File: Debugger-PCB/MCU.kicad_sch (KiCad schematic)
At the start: 12 parts, among them U5 STM32F103RCTx, Y1 12M

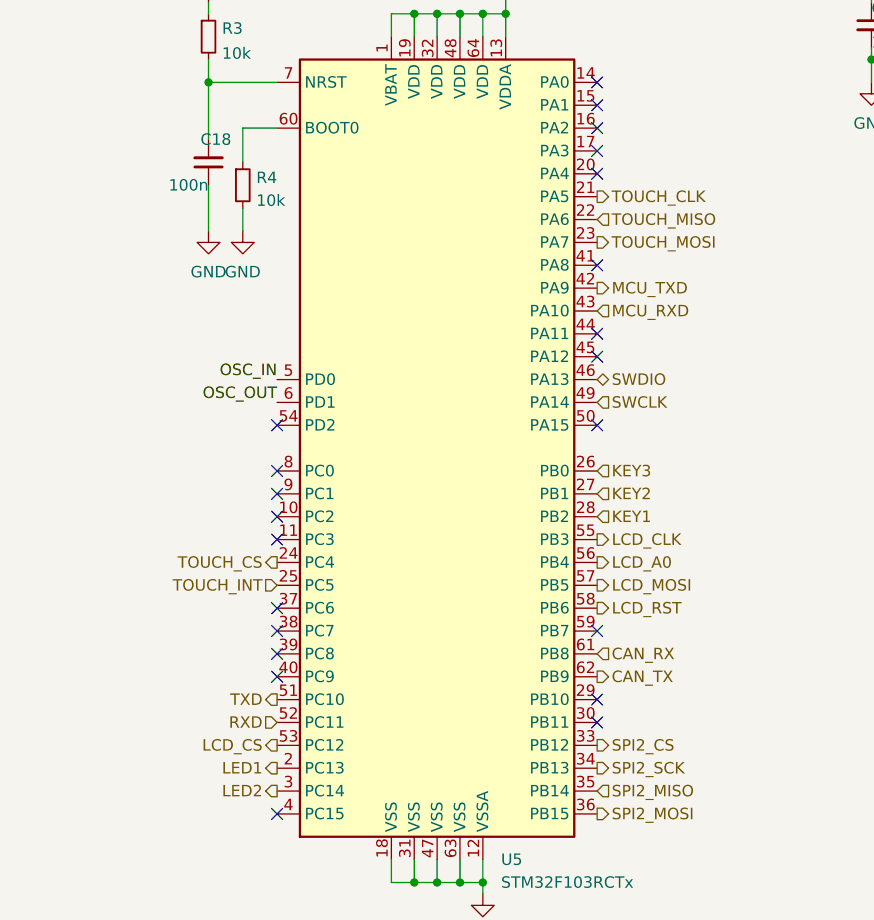
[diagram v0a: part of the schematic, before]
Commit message: fix some details of PCB
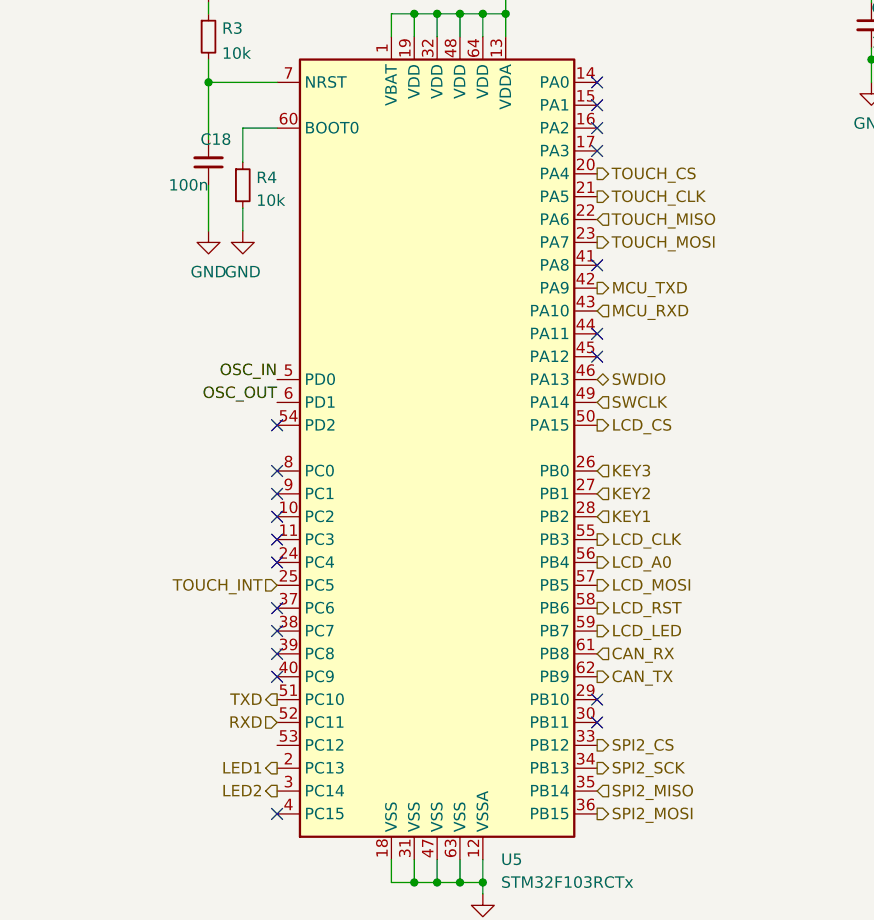
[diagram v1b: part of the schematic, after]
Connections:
- net LCD_CS: now also U5.50 (PA15); no longer U5.53 (PC12)
- net TOUCH_CS: now also U5.20 (PA4); no longer U5.24 (PC4)
- net LCD_LED: now reaches U5.59 (PB7)
- no-connect marks 22 -> 20
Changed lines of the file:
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@@
   (junction (at 134.62 43.18) (diameter 0) (color 0 0 0 0)
   )
-  (no_connect (at 152.4 111.76))
   (no_connect (at 116.84 96.52))
-  (no_connect (at 152.4 88.9))
   (no_connect (at 152.4 55.88))
   (no_connect (at 116.84 109.22))
   (no_connect (at 116.84 111.76))
+  (no_connect (at 116.84 104.14))
   (no_connect (at 116.84 101.6))
   (no_connect (at 152.4 81.28))
@@
   (no_connect (at 116.84 114.3))
   (no_connect (at 152.4 58.42))
-  (no_connect (at 152.4 60.96))
   (no_connect (at 152.4 119.38))
   (no_connect (at 116.84 93.98))
@@
     (effects (font (size 1.27 1.27)) (justify left))
   )
+  (hierarchical_label "LCD_LED" (shape output) (at 152.4 111.76 0)
+    (effects (font (size 1.27 1.27)) (justify left))
+  )
   (hierarchical_label "TXD" (shape output) (at 116.84 119.38 180)
     (effects (font (size 1.27 1.27)) (justify right))
@@
     (effects (font (size 1.27 1.27)) (justify left))
   )
+  (hierarchical_label "LCD_CS" (shape output) (at 152.4 88.9 0)
+    (effects (font (size 1.27 1.27)) (justify left))
+  )
   (hierarchical_label "SWDIO" (shape bidirectional) (at 152.4 83.82 0)
     (effects (font (size 1.27 1.27)) (justify left))
@@
     (effects (font (size 1.27 1.27)) (justify left))
   )
-  (hierarchical_label "TOUCH_CS" (shape output) (at 116.84 104.14 180)
-    (effects (font (size 1.27 1.27)) (justify right))
-  )
   (hierarchical_label "CAN_RX" (shape input) (at 152.4 114.3 0)
     (effects (font (size 1.27 1.27)) (justify left))
@@
   )
   (hierarchical_label "TOUCH_MISO" (shape input) (at 152.4 66.04 0)
+    (effects (font (size 1.27 1.27)) (justify left))
+  )
+  (hierarchical_label "TOUCH_CS" (shape output) (at 152.4 60.96 0)
     (effects (font (size 1.27 1.27)) (justify left))
   )
@@
     (effects (font (size 1.27 1.27)) (justify left))
   )
-  (hierarchical_label "LCD_CS" (shape output) (at 116.84 124.46 180)
-    (effects (font (size 1.27 1.27)) (justify right))
-  )
   (hierarchical_label "KEY1" (shape input) (at 152.4 99.06 0)

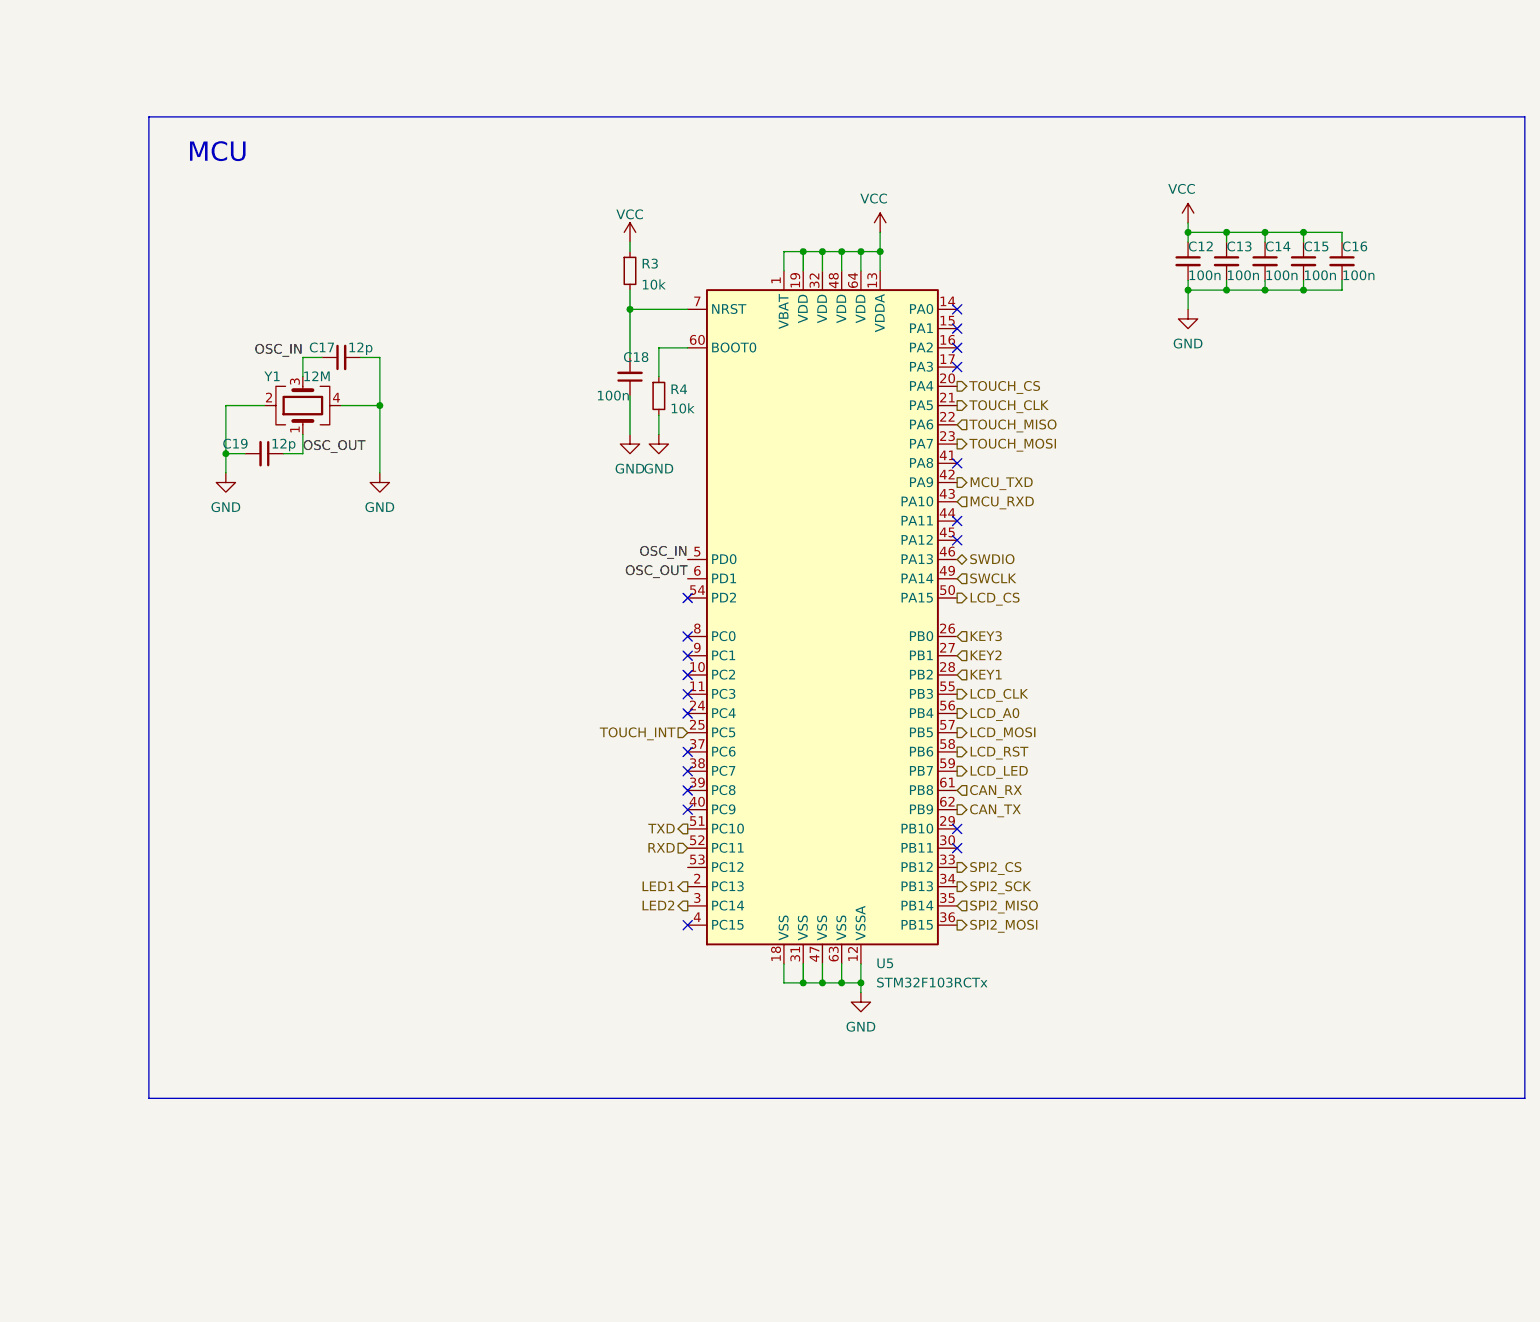
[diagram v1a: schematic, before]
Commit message: change the file name debugger-code into debugger_code_f103. Change the stm32f103rct6 into stm32f407vet6. Add file debugger_code_f407
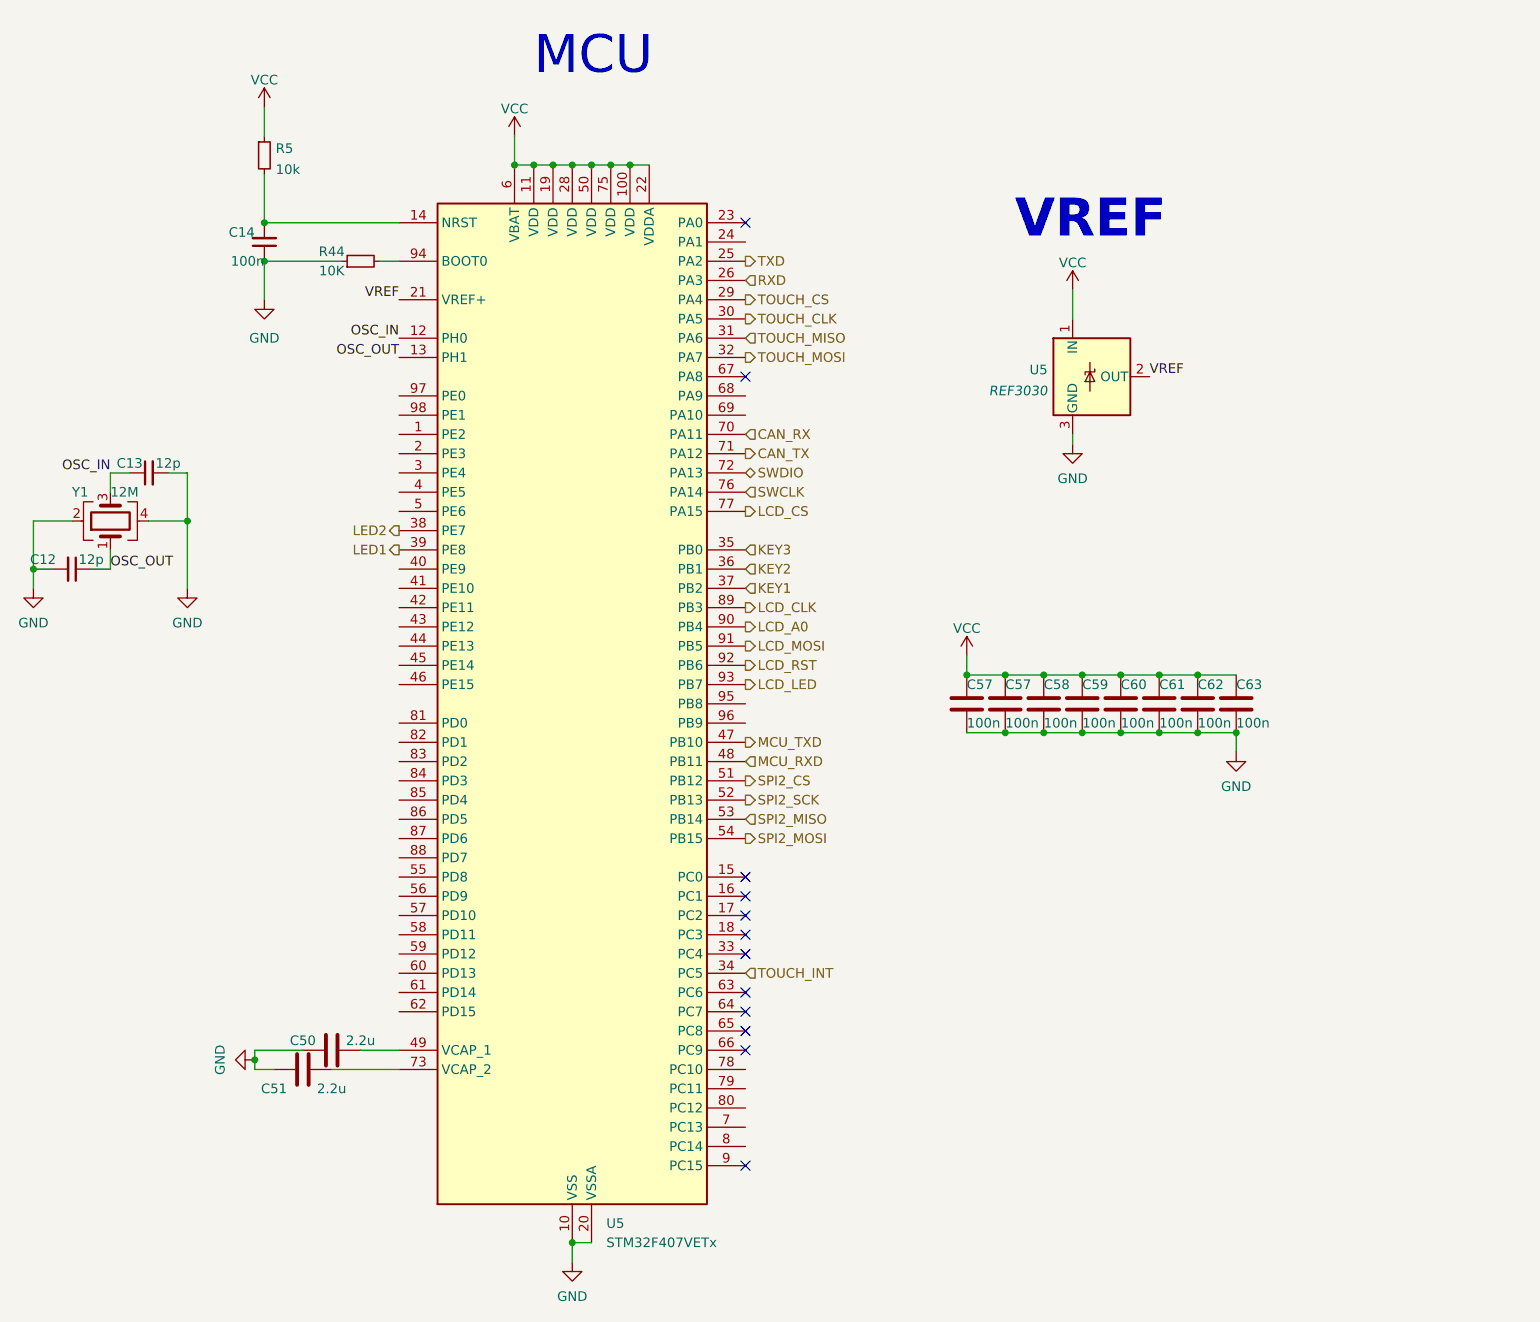
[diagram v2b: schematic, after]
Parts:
- removed C15, C16, C18: 100n, Capacitor_SMD:C_0603_1608Metric, symbol Device:C_Small
- removed C17, C19: 12p, Capacitor_SMD:C_0603_1608Metric, symbol Device:C_Small
- removed R3, R4: 10k, Resistor_SMD:R_0603_1608Metric, symbol Device:R_Small
- removed U5: STM32F103RCTx, Package_QFP:LQFP-64_10x10mm_P0.5mm, symbol MCU_ST_STM32F1:STM32F103RCTx
- added C50, C51: 2.2u, Capacitor_SMD:C_0603_1608Metric, symbol Device:C
- added C57 (x2), C58, C59, C60, C61, C62, C63: 100n, Capacitor_SMD:C_0603_1608Metric, symbol Device:C
- added R44: 10K, Resistor_SMD:R_0603_1608Metric, symbol Device:R_Small
- added R5: 10k, Resistor_SMD:R_0603_1608Metric, symbol Device:R_Small
- added U5: STM32F407VETx, Package_QFP:LQFP-100_14x14mm_P0.5mm, symbol MCU_ST_STM32F4:STM32F407VETx
- added U5: REF3030, Package_TO_SOT_SMD:SOT-23, symbol Reference_Voltage:REF3030
- C12, C13: value 100n -> 12p
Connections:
- net CAN_RX: now also U5.70 (PA11)
- net CAN_TX: now also U5.71 (PA12)
- net GND: now also C14.1, C50.1, C51.1, C57.2, C57.2, C58.2, C59.2, C60.2, C61.2, C62.2, C63.2, R44.1, U5.10 (VSS), U5.20 (VSSA), U5.27 (VSS), U5.3 (GND), U5.74 (VSS), U5.99 (VSS); no longer C14.2
- net KEY1: now also U5.37 (PB2)
- net KEY2: now also U5.36 (PB1)
- net KEY3: now also U5.35 (PB0)
- net LCD_A0: now also U5.90 (PB4)
- net LCD_CLK: now also U5.89 (PB3)
- net LCD_CS: now also U5.77 (PA15)
- net LCD_LED: now also U5.93 (PB7)
- net LCD_MOSI: now also U5.91 (PB5)
- net LCD_RST: now also U5.92 (PB6)
- net LED1: now also U5.39 (PE8)
- net LED2: now also U5.38 (PE7)
- net MCU_RXD: now also U5.48 (PB11)
- net MCU_TXD: now also U5.47 (PB10)
- net OSC_IN: now also C13.1, U5.12 (PH0)
- net OSC_OUT: now also C12.1, U5.13 (PH1)
- net RXD: now also U5.26 (PA3)
- net SPI2_CS: now also U5.51 (PB12)
- net SPI2_MISO: now also U5.53 (PB14)
- net SPI2_MOSI: now also U5.54 (PB15)
- net SPI2_SCK: now also U5.52 (PB13)
- net SWCLK: now also U5.76 (PA14)
- net SWDIO: now also U5.72 (PA13)
- net TOUCH_CLK: now also U5.30 (PA5)
- net TOUCH_CS: now also U5.29 (PA4)
- net TOUCH_INT: now also U5.34 (PC5)
- net TOUCH_MISO: now also U5.31 (PA6)
- net TOUCH_MOSI: now also U5.32 (PA7)
- net TXD: now also U5.25 (PA2)
- net VCC: now also C57.1, C57.1, C58.1, C59.1, C60.1, C61.1, C62.1, C63.1, R5.1, U5.1 (IN), U5.100 (VDD), U5.11 (VDD), U5.19 (VDD), U5.22 (VDDA), U5.28 (VDD), U5.50 (VDD), U5.6 (VBAT), U5.75 (VDD); no longer C12.1, C13.1, C14.1
- new net: C14.2, R5.2, U5.14 (NRST)
- new net: C50.2, U5.49 (VCAP_1)
- new net: C51.2, U5.73 (VCAP_2)
- new net: R44.2, U5.94 (BOOT0)
- new net VREF: U5.2 (OUT), U5.21 (VREF+)
- no-connect marks 20 -> 12
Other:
- note added: "VREF"

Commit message: temp.change the PCB.And change the code.
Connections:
- net LCD_CS: now also U5.95 (PB8)
- net RESET: now reaches C14.2, R5.2, U5.14 (NRST)
- net LCD_CS0: now reaches U5.15 (PC0)
- net ADC1_IN11: now reaches U5.16 (PC1)
- net ADC1_IN12: now reaches U5.17 (PC2)
- net ADC1_IN13: now reaches U5.18 (PC3)
- net ADC1_IN0: now reaches U5.23 (PA0)
- net ADC1_IN1: now reaches U5.24 (PA1)
- net ADC1_IN14: now reaches U5.33 (PC4)
- net TIM1_CH1: now reaches U5.40 (PE9)
- net TIM1_CH2: now reaches U5.42 (PE11)
- net I2C3_SDA: now reaches U5.56 (PD9)
- net TIM4_CH2: now reaches U5.59 (PD12)
- net TIM4_CH1: now reaches U5.60 (PD13)
- net TIM3_CH1: now reaches U5.63 (PC6)
- net TIM3_CH2: now reaches U5.64 (PC7)
- net I2C3_SCL: now reaches U5.67 (PA8)
- net KEY5: now reaches U5.68 (PA9)
- net KEY4: now reaches U5.69 (PA10)
- net LCD_DC: now reaches U5.96 (PB9)
- no-connect marks 12 -> 3
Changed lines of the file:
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@@
   (junction (at 173.99 99.06) (diameter 0) (color 0 0 0 0)
   )
-  (no_connect (at 124.46 133.35))
   (no_connect (at 124.46 148.59))
-  (no_connect (at 124.46 39.37))
   (no_connect (at 124.46 146.05))
   (no_connect (at 124.46 163.83))
-  (no_connect (at 124.46 59.69))
-  (no_connect (at 124.46 125.73))
-  (no_connect (at 124.46 140.97))
-  (no_connect (at 124.46 128.27))
-  (no_connect (at 124.46 143.51))
-  (no_connect (at 124.46 135.89))
-  (no_connect (at 124.46 130.81))
   (wire (pts (xy 184.15 106.68) (xy 189.23 106.68))
     (stroke (width 0) (type default))
@@
     (effects (font (size 1.27 1.27)) (justify left))
   )
+  (hierarchical_label "ADC1_IN1" (shape input) (at 124.46 41.91 0) (fields_autoplaced)
+    (effects (font (size 1.27 1.27)) (justify left))
+  )
+  (hierarchical_label "I2C3_SCL" (shape output) (at 124.46 59.69 0) (fields_autoplaced)
+    (effects (font (size 1.27 1.27)) (justify left))
+  )
   (hierarchical_label "SWDIO" (shape bidirectional) (at 124.46 72.39 0) (fields_autoplaced)
     (effects (font (size 1.27 1.27)) (justify left))
@@
     (effects (font (size 1.27 1.27)) (justify left))
   )
+  (hierarchical_label "TIM3_CH1" (shape input) (at 124.46 140.97 0) (fields_autoplaced)
+    (effects (font (size 1.27 1.27)) (justify left))
+  )
+  (hierarchical_label "LCD_DC" (shape output) (at 124.46 105.41 0) (fields_autoplaced)
+    (effects (font (size 1.27 1.27)) (justify left))
+  )
+  (hierarchical_label "KEY5" (shape input) (at 124.46 62.23 0) (fields_autoplaced)
+    (effects (font (size 1.27 1.27)) (justify left))
+  )
+  (hierarchical_label "ADC1_IN14" (shape input) (at 124.46 135.89 0) (fields_autoplaced)
+    (effects (font (size 1.27 1.27)) (justify left))
+  )
+  (hierarchical_label "ADC1_IN13" (shape input) (at 124.46 133.35 0) (fields_autoplaced)
+    (effects (font (size 1.27 1.27)) (justify left))
+  )
   (hierarchical_label "MCU_TXD" (shape output) (at 124.46 107.95 0) (fields_autoplaced)
     (effects (font (size 1.27 1.27)) (justify left))
@@
     (effects (font (size 1.27 1.27)) (justify left))
   )
+  (hierarchical_label "I2C3_SDA" (shape bidirectional) (at 78.74 128.27 180) (fields_autoplaced)
+    (effects (font (size 1.27 1.27)) (justify right))
+  )
+  (hierarchical_label "RESET" (shape input) (at 60.96 39.37 180) (fields_autoplaced)
+    (effects (font (size 1.27 1.27)) (justify right))
+  )
   (hierarchical_label "TOUCH_CS" (shape output) (at 124.46 49.53 0) (fields_autoplaced)
     (effects (font (size 1.27 1.27)) (justify left))
@@
     (effects (font (size 1.27 1.27)) (justify right))
   )
+  (hierarchical_label "ADC1_IN11" (shape input) (at 124.46 128.27 0) (fields_autoplaced)
+    (effects (font (size 1.27 1.27)) (justify left))
+  )
+  (hierarchical_label "ADC1_IN12" (shape input) (at 124.46 130.81 0) (fields_autoplaced)
+    (effects (font (size 1.27 1.27)) (justify left))
+  )
   (hierarchical_label "KEY1" (shape input) (at 124.46 87.63 0) (fields_autoplaced)
     (effects (font (size 1.27 1.27)) (justify left))
   )
+  (hierarchical_label "KEY4" (shape input) (at 124.46 64.77 0) (fields_autoplaced)
+    (effects (font (size 1.27 1.27)) (justify left))
+  )
   (hierarchical_label "CAN_TX" (shape output) (at 124.46 69.85 0) (fields_autoplaced)
     (effects (font (size 1.27 1.27)) (justify left))
@@
     (effects (font (size 1.27 1.27)) (justify left))
   )
+  (hierarchical_label "TIM4_CH1" (shape input) (at 78.74 138.43 180) (fields_autoplaced)
+    (effects (font (size 1.27 1.27)) (justify right))
+  )
   (hierarchical_label "LCD_CS" (shape output) (at 124.46 77.47 0) (fields_autoplaced)
     (effects (font (size 1.27 1.27)) (justify left))
   )
+  (hierarchical_label "LCD_CS0" (shape output) (at 124.46 125.73 0) (fields_autoplaced)
+    (effects (font (size 1.27 1.27)) (justify left))
+  )
   (hierarchical_label "TOUCH_CLK" (shape output) (at 124.46 52.07 0) (fields_autoplaced)
     (effects (font (size 1.27 1.27)) (justify left))
   )
+  (hierarchical_label "LCD_CS" (shape output) (at 124.46 102.87 0) (fields_autoplaced)
+    (effects (font (size 1.27 1.27)) (justify left))
+  )
   (hierarchical_label "TOUCH_MOSI" (shape output) (at 124.46 57.15 0) (fields_autoplaced)
     (effects (font (size 1.27 1.27)) (justify left))
@@
     (effects (font (size 1.27 1.27)) (justify left))
   )
+  (hierarchical_label "TIM1_CH2" (shape input) (at 78.74 90.17 180) (fields_autoplaced)
+    (effects (font (size 1.27 1.27)) (justify right))
+  )
+  (hierarchical_label "TIM3_CH2" (shape input) (at 124.46 143.51 0) (fields_autoplaced)
+    (effects (font (size 1.27 1.27)) (justify left))
+  )
+  (hierarchical_label "ADC1_IN0" (shape input) (at 124.46 39.37 0) (fields_autoplaced)
+    (effects (font (size 1.27 1.27)) (justify left))
+  )
   (hierarchical_label "LED2" (shape output) (at 78.74 80.01 180) (fields_autoplaced)
     (effects (font (size 1.27 1.27)) (justify right))
   )
+  (hierarchical_label "TIM4_CH2" (shape input) (at 78.74 135.89 180) (fields_autoplaced)
+    (effects (font (size 1.27 1.27)) (justify right))
+  )
   (hierarchical_label "SPI2_MISO" (shape input) (at 124.46 118.11 0) (fields_autoplaced)
     (effects (font (size 1.27 1.27)) (justify left))
   )
+  (hierarchical_label "TIM1_CH1" (shape input) (at 78.74 85.09 180) (fields_autoplaced)
+    (effects (font (size 1.27 1.27)) (justify right))
+  )
   (symbol (lib_id "MCU_ST_STM32F4:STM32F407VETx") (at 101.6 102.87 0) (unit 1)
